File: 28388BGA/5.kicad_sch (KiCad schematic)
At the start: 43 parts, among them Q15 TXB0104PWR, Q16 TPS27082LDDCR, Q17 TPT75176B-SO1R, Q18 TPT75176B-SO1R

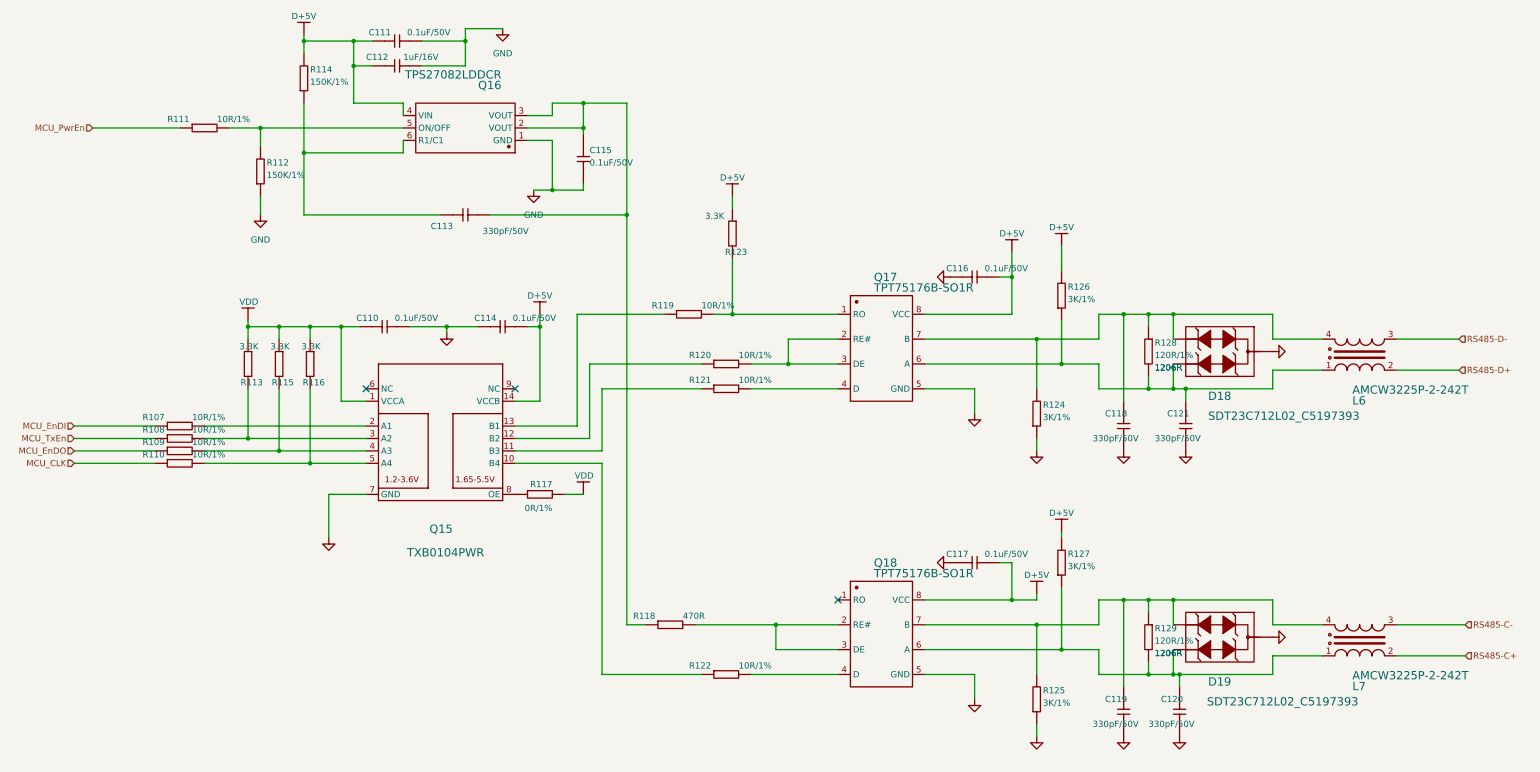
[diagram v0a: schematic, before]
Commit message: 修复AGND BUG
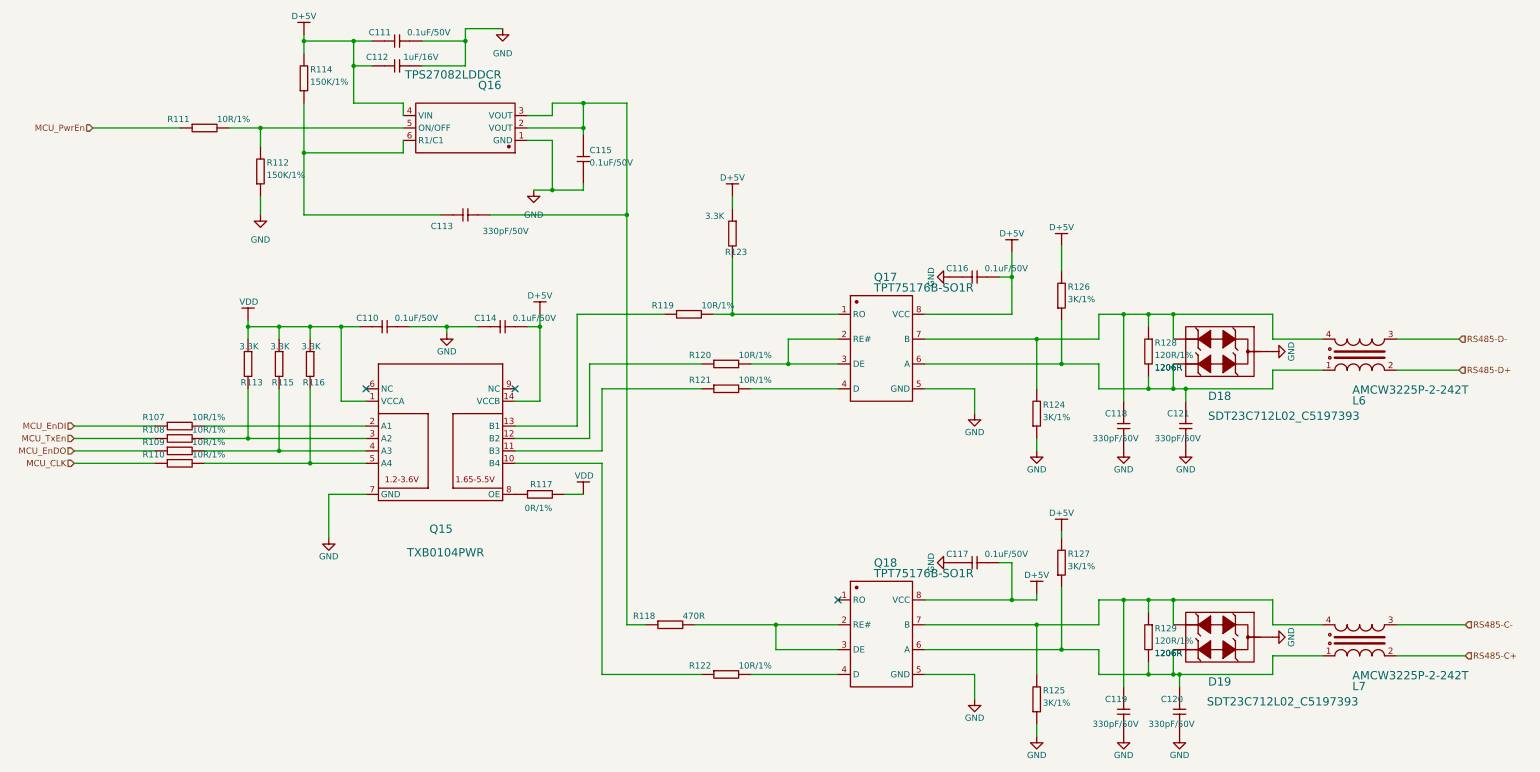
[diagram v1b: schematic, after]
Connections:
- net AGND is gone; now on net GND: C110.2, C114.1, C116.1, C117.1, C118.2, C119.2, C120.2, C121.2, D18.3, D19.3, Q15.7 (GND), Q17.5 (GND), Q18.5 (GND), R124.1, R125.1
